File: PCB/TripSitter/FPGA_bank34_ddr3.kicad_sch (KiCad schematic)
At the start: 12 parts, among them U1 XC7A100T-FGG484, U3 IS62WVS2568FBLL-20NLI

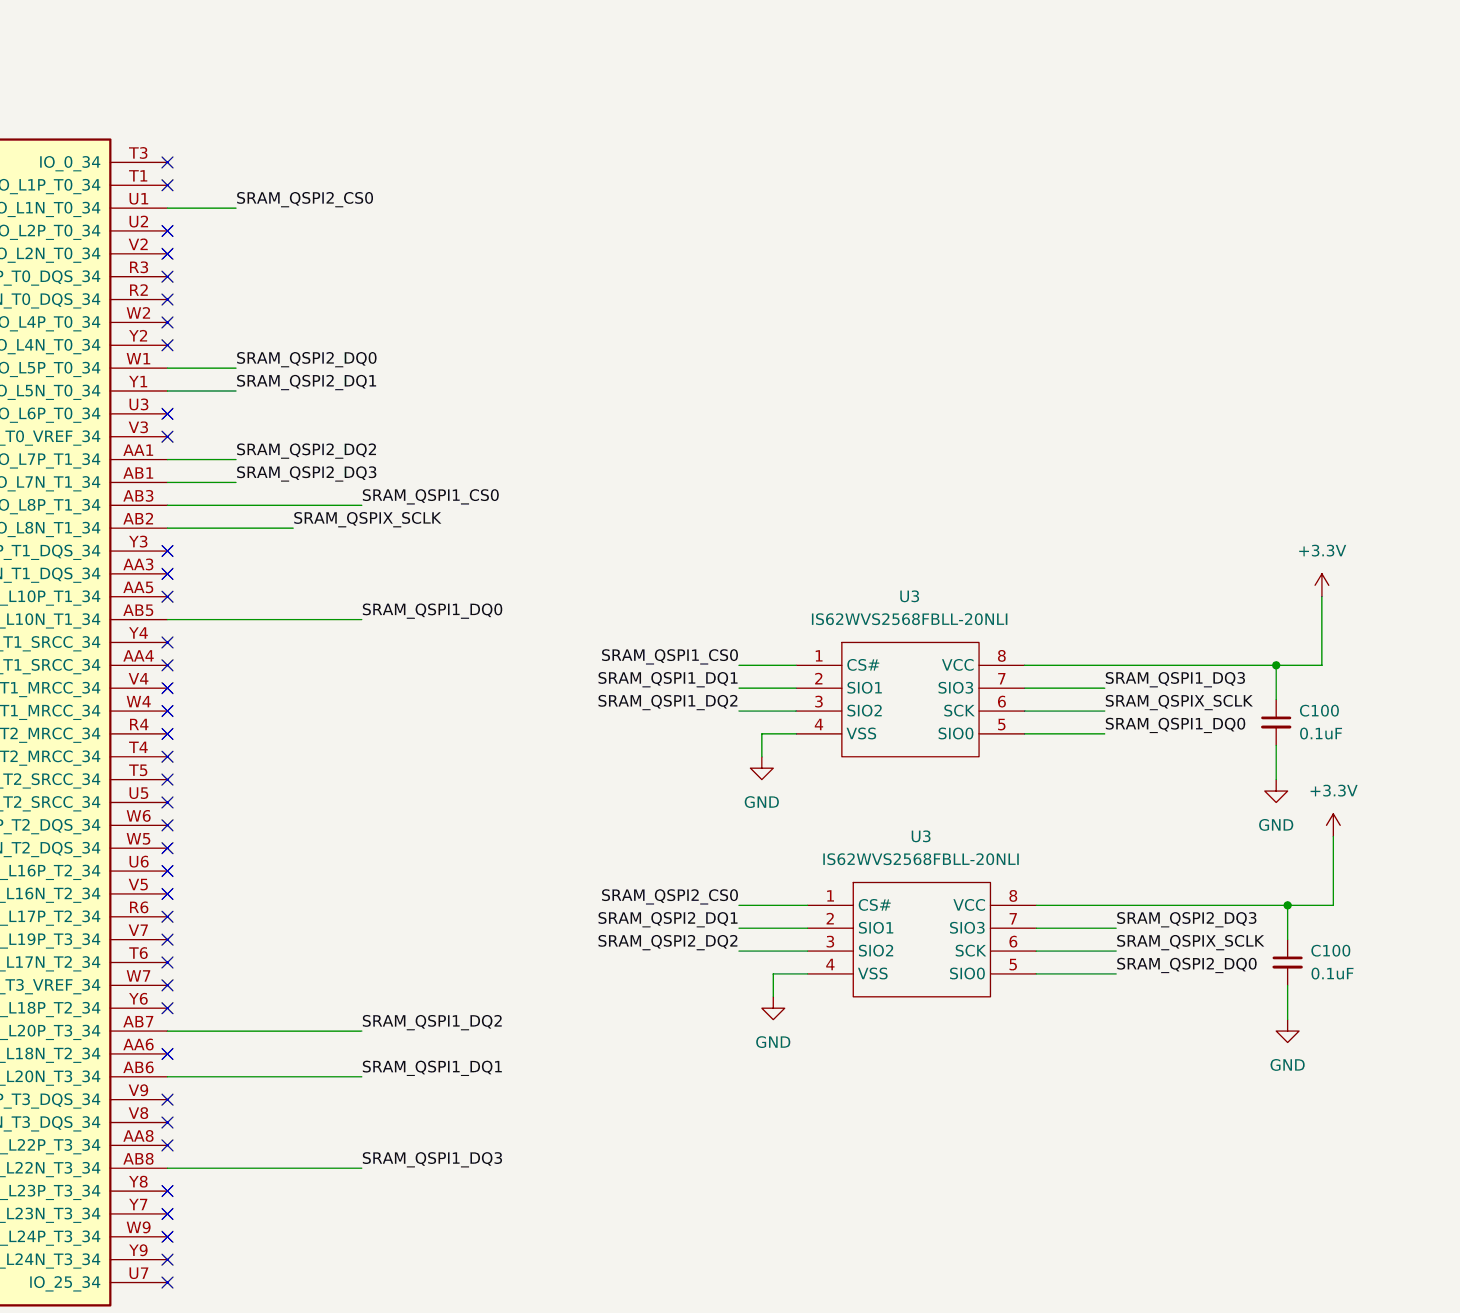
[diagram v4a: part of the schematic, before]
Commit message: pcb: Add debug leds and pinout header for FPGA
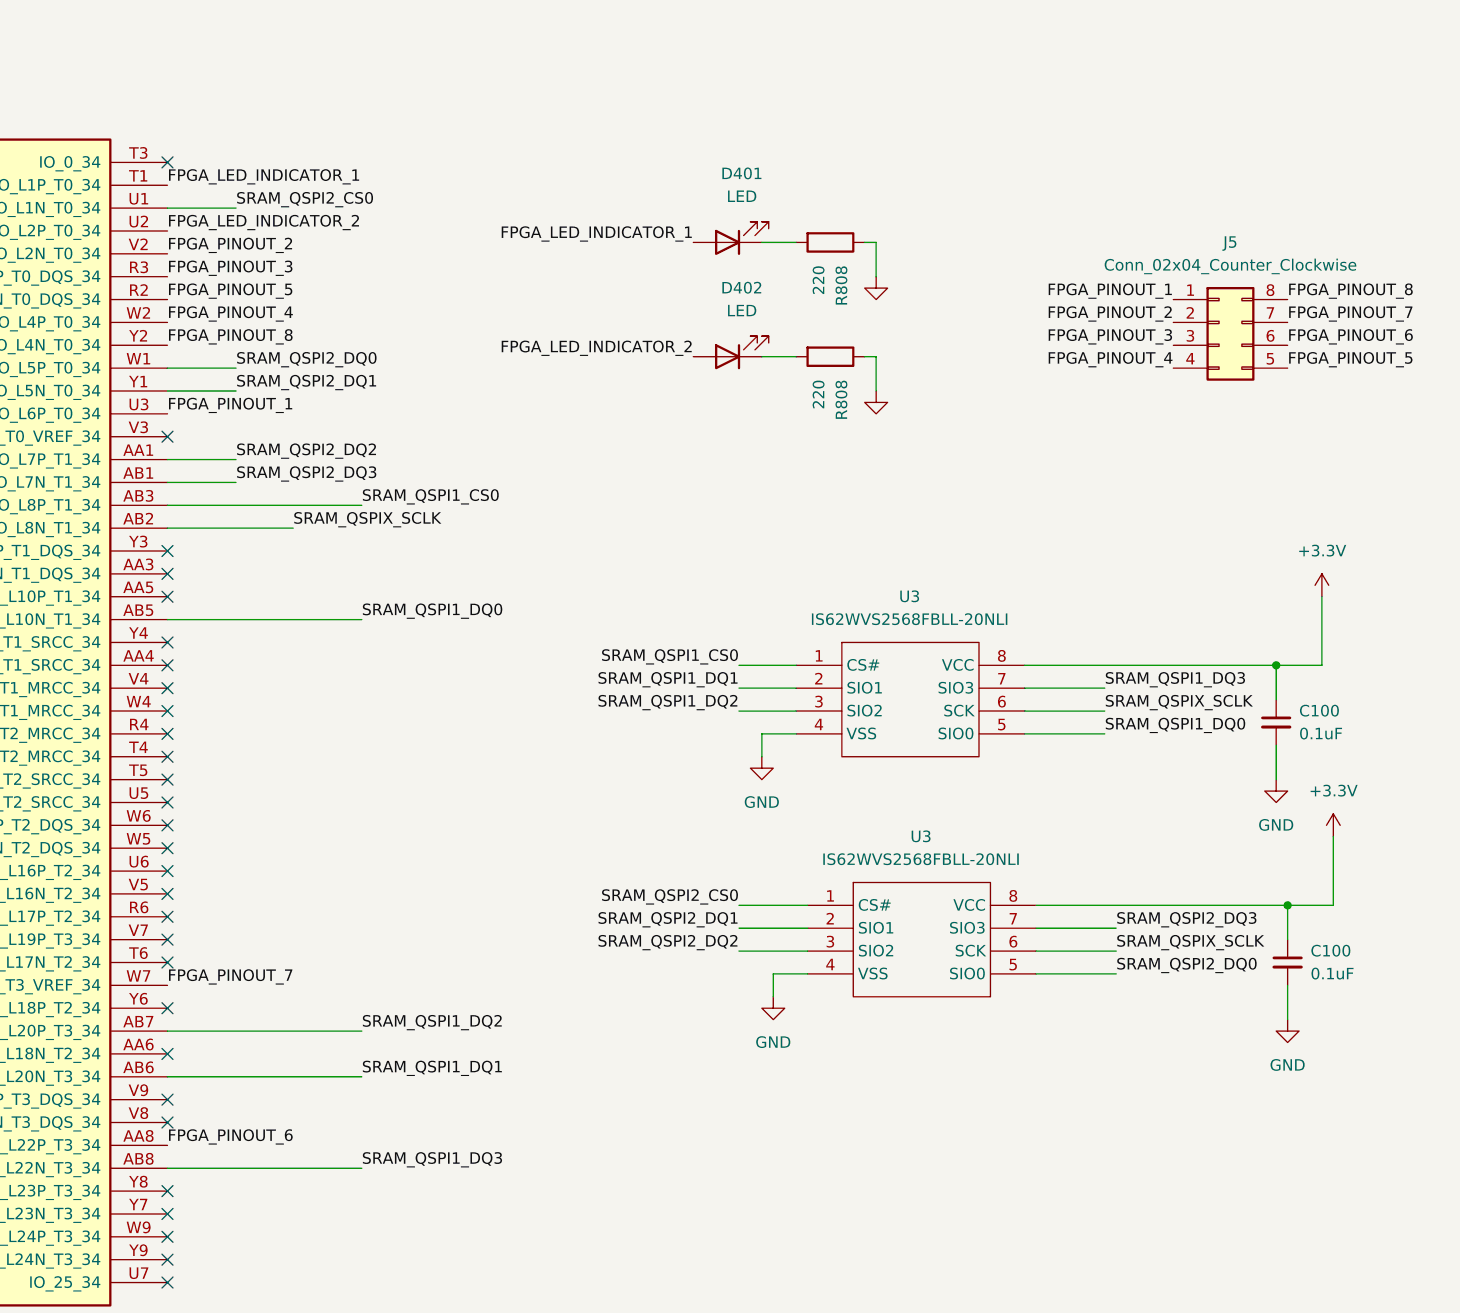
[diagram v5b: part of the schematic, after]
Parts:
- added D401, D402: LED, LED_SMD:LED_1206_3216Metric_Pad1.42x1.75mm_HandSolder, symbol Device:LED
- added J5: Conn_02x04_Counter_Clockwise, Connector_PinHeader_2.00mm:PinHeader_2x04_P2.00mm_Vertical, symbol Connector_Generic:Conn_02x04_Counter_Clockwise
- added R808 (x2): 220, Resistor_SMD:R_0805_2012Metric_Pad1.20x1.40mm_HandSolder, symbol Device:R
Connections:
- net GND: now also R808.1, R808.1
- net FPGA_PINOUT_6: now reaches U1.AA8 (IO_L22P_T3_34)
- net FPGA_PINOUT_6: now also J5.6 (Pin_6)
- net FPGA_PINOUT_5: now reaches U1.R2 (IO_L3N_T0_DQS_34)
- net FPGA_PINOUT_5: now also J5.5 (Pin_5)
- net FPGA_PINOUT_3: now reaches U1.R3 (IO_L3P_T0_DQS_34)
- net FPGA_PINOUT_3: now also J5.3 (Pin_3)
- net FPGA_LED_INDICATOR_1: now reaches U1.T1 (IO_L1P_T0_34)
- net FPGA_LED_INDICATOR_1: now also D401.2 (A)
- net FPGA_LED_INDICATOR_2: now reaches U1.U2 (IO_L2P_T0_34)
- net FPGA_LED_INDICATOR_2: now also D402.2 (A)
- net FPGA_PINOUT_1: now reaches U1.U3 (IO_L6P_T0_34)
- net FPGA_PINOUT_1: now also J5.1 (Pin_1)
- net FPGA_PINOUT_2: now reaches U1.V2 (IO_L2N_T0_34)
- net FPGA_PINOUT_2: now also J5.2 (Pin_2)
- net FPGA_PINOUT_4: now reaches U1.W2 (IO_L4P_T0_34)
- net FPGA_PINOUT_4: now also J5.4 (Pin_4)
- net FPGA_PINOUT_7: now reaches U1.W7 (IO_L19N_T3_VREF_34)
- net FPGA_PINOUT_7: now also J5.7 (Pin_7)
- net FPGA_PINOUT_8: now reaches U1.Y2 (IO_L4N_T0_34)
- net FPGA_PINOUT_8: now also J5.8 (Pin_8)
- new net: D401.1 (K), R808.2
- new net: D402.1 (K), R808.2
- no-connect marks 95 -> 85
